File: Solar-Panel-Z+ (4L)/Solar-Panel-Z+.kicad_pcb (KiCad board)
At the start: 4 copper layers, 48.4 x 48.4 mm, 79 parts, among them J1 FTS-105-01-L-DV-A, Q1 BSS138DWQ-7, Q2 MBT2222ADW1T1, Q3 BSS138DWQ-7, Q4 MBT2222ADW1T1, U1 BQ25570RGRR, U2 TSL2561

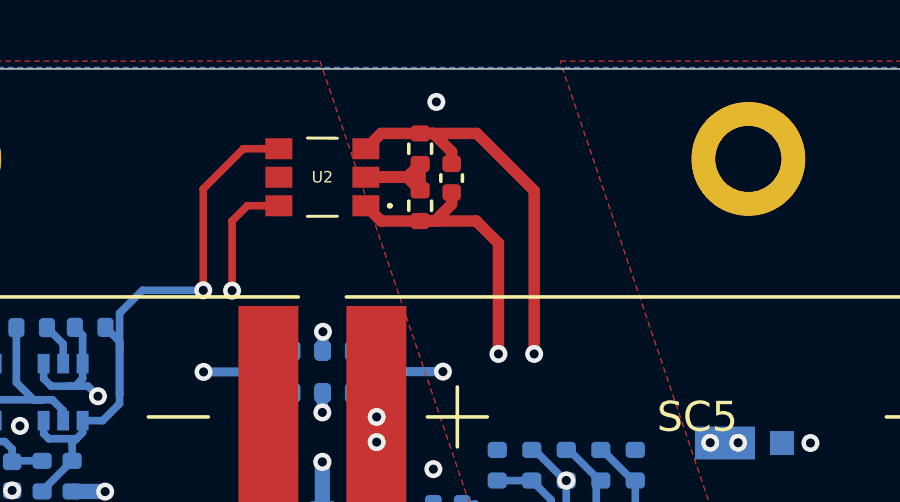
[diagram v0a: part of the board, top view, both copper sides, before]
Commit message: Added 4 Layer Z- board
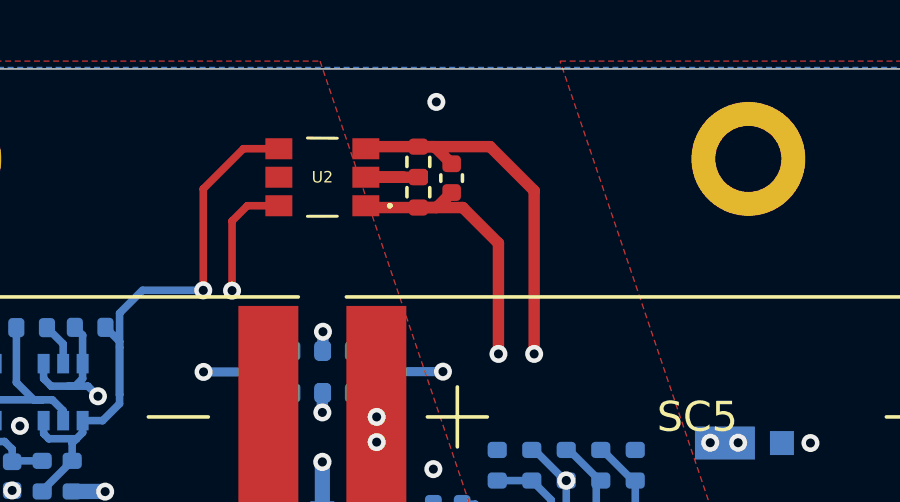
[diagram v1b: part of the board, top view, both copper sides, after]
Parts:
- moved R1 0.45 mm to (109.9, 46.4)
- moved R2 0.44 mm to (109.9, 45.4)
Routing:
- net Net-(R1-Pad1): track 4.71 -> 2.96 mm
- net GND: track 31.1 -> 30.4 mm
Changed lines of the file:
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@@
   )
   (footprint "Resistor_SMD:R_0402_1005Metric" (layer "F.Cu")
-    (at 109.96 46.86 -90)
+    (at 109.9 46.41 -90)
     (descr "Resistor SMD 0402 (1005 Metric), square (rectangular) end terminal, IPC_7351 nominal, (Body size source: IPC-SM-782 page 72, https://www.pcb-3d.com/wordpress/wp-content/uploads/ipc-sm-782a_amendment_1_and_2.pdf), generated with kicad-footprint-generator")
     (tags "resistor")
@@
   )
   (footprint "Resistor_SMD:R_0402_1005Metric" (layer "F.Cu")
-    (at 109.96 44.96 -90)
+    (at 109.9 45.4 -90)
     (descr "Resistor SMD 0402 (1005 Metric), square (rectangular) end terminal, IPC_7351 nominal, (Body size source: IPC-SM-782 page 72, https://www.pcb-3d.com/wordpress/wp-content/uploads/ipc-sm-782a_amendment_1_and_2.pdf), generated with kicad-footprint-generator")
     (tags "resistor")
@@
     (pts (xy 82.5 42.3) (xy 82.5 90.7))
     (height 2.1)
-    (gr_text "48.4000 mm" (at 79.25 66.5 90) (layer "Dwgs.User")
+    (gr_text "1905.5118 mils" (at 79.25 66.5 90) (layer "Dwgs.User")
       (effects (font (size 1 1) (thickness 0.15)))
     )
@@
     (pts (xy 82.5 42.3) (xy 130.9 42.3))
     (height -2.1)
-    (gr_text "48.4000 mm" (at 106.7 39.05) (layer "Dwgs.User")
+    (gr_text "1905.5118 mils" (at 106.7 39.05) (layer "Dwgs.User")
       (effects (font (size 1 1) (thickness 0.15)))
     )
@@
     (style (thickness 0.1) (arrow_length 1.27) (text_position_mode 0) (extension_height 0.58642) (extension_offset 0.5) keep_text_aligned)
   )
+  (segment (start 113.76 51.8) (end 113.76 46.36) (width 0.381) (layer "F.Cu") (net 1))
   (segment (start 83.9 78.7) (end 89.5 78.7) (width 0.762) (layer "F.Cu") (net 1))
-  (segment (start 108.66 44.45) (end 108.15 44.96) (width 0.381) (layer "F.Cu") (net 1))
-  (segment (start 109.96 44.45) (end 108.66 44.45) (width 0.381) (layer "F.Cu") (net 1))
-  (segment (start 113.76 46.36) (end 111.85 44.45) (width 0.381) (layer "F.Cu") (net 1))
   (segment (start 89.5 78.7) (end 91.1 78.7) (width 0.762) (layer "F.Cu") (net 1))
-  (segment (start 111.01 45.06) (end 110.4 44.45) (width 0.381) (layer "F.Cu") (net 1))
-  (segment (start 111.85 44.45) (end 109.96 44.45) (width 0.381) (layer "F.Cu") (net 1))
-  (segment (start 110.4 44.45) (end 109.96 44.45) (width 0.381) (layer "F.Cu") (net 1))
-  (segment (start 113.76 51.8) (end 113.76 46.36) (width 0.381) (layer "F.Cu") (net 1))
+  (segment (start 108.22 44.89) (end 108.15 44.96) (width 0.381) (layer "F.Cu") (net 1))
+  (segment (start 110.44 44.89) (end 109.9 44.89) (width 0.381) (layer "F.Cu") (net 1))
+  (segment (start 111.01 45.46) (end 110.44 44.89) (width 0.381) (layer "F.Cu") (net 1))
+  (segment (start 112.29 44.89) (end 109.9 44.89) (width 0.381) (layer "F.Cu") (net 1))
+  (segment (start 113.76 46.36) (end 112.29 44.89) (width 0.381) (layer "F.Cu") (net 1))
   (segment (start 90.2 78.7) (end 92 78.7) (width 0.762) (layer "F.Cu") (net 1))
+  (segment (start 109.9 44.89) (end 108.22 44.89) (width 0.381) (layer "F.Cu") (net 1))
   (segment (start 89.5 78.7) (end 90.2 78.7) (width 0.762) (layer "F.Cu") (net 1))
-  (segment (start 111.01 45.46) (end 111.01 45.06) (width 0.381) (layer "F.Cu") (net 1))
   (via (at 116.17 65.71) (size 0.6) (drill 0.3) (layers "F.Cu" "B.Cu") (free) (net 1))
   (via (at 92 78.7) (size 0.6096) (drill 0.3048) (layers "F.Cu" "B.Cu") (net 1))
@@
   (segment (start 113.158911 60.373245) (end 113.858911 60.373245) (width 0.254) (layer "B.Cu") (net 1))
   (segment (start 116.501089 60.373245) (end 115.801089 60.373245) (width 0.254) (layer "B.Cu") (net 1))
-  (segment (start 110.45 47.37) (end 109.96 47.37) (width 0.381) (layer "F.Cu") (net 2))
-  (segment (start 112.57 48.11) (end 111.83 47.37) (width 0.381) (layer "F.Cu") (net 2))
-  (segment (start 111.01 46.42) (end 111.01 46.81) (width 0.381) (layer "F.Cu") (net 2))
   (segment (start 112.57 51.8) (end 112.57 48.11) (width 0.381) (layer "F.Cu") (net 2))
-  (segment (start 111.83 47.37) (end 109.96 47.37) (width 0.381) (layer "F.Cu") (net 2))
-  (segment (start 108.66 47.37) (end 108.15 46.86) (width 0.381) (layer "F.Cu") (net 2))
-  (segment (start 109.96 47.37) (end 108.66 47.37) (width 0.381) (layer "F.Cu") (net 2))
-  (segment (start 111.01 46.81) (end 110.45 47.37) (width 0.381) (layer "F.Cu") (net 2))
+  (segment (start 111.01 46.42) (end 110.51 46.92) (width 0.381) (layer "F.Cu") (net 2))
+  (segment (start 111.38 46.92) (end 108.21 46.92) (width 0.381) (layer "F.Cu") (net 2))
+  (segment (start 110.51 46.92) (end 109.9 46.92) (width 0.381) (layer "F.Cu") (net 2))
+  (segment (start 112.57 48.11) (end 111.38 46.92) (width 0.381) (layer "F.Cu") (net 2))
+  (segment (start 108.21 46.92) (end 108.15 46.86) (width 0.381) (layer "F.Cu") (net 2))
   (via (at 99.46 56.39) (size 0.6) (drill 0.3) (layers "F.Cu" "B.Cu") (net 2))
   (via (at 112.57 51.8) (size 0.6) (drill 0.3) (layers "F.Cu" "B.Cu") (net 2))
@@
   (segment (start 98.66 61.89) (end 99.52 61.03) (width 0.254) (layer "B.Cu") (net 37))
   (segment (start 97.36 62.386089) (end 97.36 61.89) (width 0.254) (layer "B.Cu") (net 37))
-  (segment (start 109.52 45.91) (end 108.15 45.91) (width 0.381) (layer "F.Cu") (net 38))
-  (segment (start 109.96 45.47) (end 109.96 46.35) (width 0.381) (layer "F.Cu") (net 38))
-  (segment (start 109.96 46.35) (end 109.52 45.91) (width 0.381) (layer "F.Cu") (net 38))
+  (segment (start 109.9 45.91) (end 108.15 45.91) (width 0.381) (layer "F.Cu") (net 38))
   (segment (start 109.419997 45.910003) (end 108.209203 45.910003) (width 0.381) (layer "F.Cu") (net 38))
-  (segment (start 109.96 45.47) (end 109.519997 45.910003) (width 0.381) (layer "F.Cu") (net 38))
   (via (at 92.65 70.95) (size 0.6096) (drill 0.3048) (layers "F.Cu" "B.Cu") (net 40))
   (via (at 114.27 63.38) (size 0.6096) (drill 0.3048) (layers "F.Cu" "B.Cu") (net 40))

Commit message: Z board updates
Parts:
- moved TP1 0.79 mm to (120.9, 77.1)
- moved TP3 0.79 mm to (120.9, 70.1)
- moved TP2 0.79 mm to (120.9, 74.7)
- moved TP4 0.79 mm to (120.9, 72.4)
- moved R16 0.32 mm to (112.0, 67.8)
- moved C2 0.10 mm to (106.7, 67.3)
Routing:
- net GND: track 30.4 -> 23.5 mm
- net VBAT: track 46.1 -> 43.9 mm
- net SCL_LS: track 21.0 -> 19.1 mm
- net Net-(R14-Pad1): track 12.9 -> 12.3 mm
- net Net-(C7-Pad1): track 0.59 -> 0.00 mm
- net /VSOLAR_FULL: track 26.9 -> 26.4 mm
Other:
- board text added: "[BAT <-> USB]"

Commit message: Exported Gerbers
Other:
- board text added: "08-AUG-2022"
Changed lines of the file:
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@@
       (drillshape 0)
       (scaleselection 1)
-      (outputdirectory "../../Z+/")
+      (outputdirectory "../gerbers/Gerbers Z+ (4L) (08-08-2022)/")
     )
   )
@@
     (effects (font (size 1.143 1.143) (thickness 0.2032)) (justify mirror))
   )
+  (gr_text "08-AUG-2022" (at 112.395 85.4456) (layer "B.SilkS")
+    (effects (font (size 0.508 0.508) (thickness 0.1016)) (justify mirror))
+  )
   (gr_text "Cable Pinout\n1.BATT_P\n2.VUSB\n3.BURN1\n4.BURN2\n5.COIL_P\n6.COIL_N\n7.SDA\n8.SCL\n9.+3V3\n10.GND" (at 90.3 70.5) (layer "B.SilkS")
     (effects (font (size 0.635 0.635) (thickness 0.0762)) (justify left mirror))
@@
   (segment (start 114.830005 61.102156) (end 114.830005 61.89) (width 0.3048) (layer "B.Cu") (net 40))
   (zone (net 26) (net_name "Net-(D3-Pad1)") (layer "F.Cu") (hatch edge 0.508)
-    (connect_pads yes (clearance 0.127))
+    (connect_pads yes (clearance 0.1524))
     (min_thickness 0.254) (filled_areas_thickness no)
     (fill yes (thermal_gap 0.508) (thermal_bridge_width 0.508))
@@
   )
   (zone (net 23) (net_name "/VSOLAR_FULL") (layer "F.Cu") (hatch edge 0.508)
-    (connect_pads yes (clearance 0.127))
+    (connect_pads yes (clearance 0.1524))
     (min_thickness 0.254) (filled_areas_thickness no)
     (fill yes (thermal_gap 0.508) (thermal_bridge_width 0.508))
@@
   )
   (zone (net 1) (net_name "GND") (layer "F.Cu") (hatch edge 0.508)
-    (connect_pads yes (clearance 0.127))
+    (connect_pads yes (clearance 0.1524))
     (min_thickness 0.254) (filled_areas_thickness no)
     (fill yes (thermal_gap 0.508) (thermal_bridge_width 0.508))
@@
   )
   (zone (net 2) (net_name "+3V3") (layer "In1.Cu") (hatch edge 0.508)
-    (connect_pads yes (clearance 0))
+    (connect_pads yes (clearance 0.1524))
     (min_thickness 0.254) (filled_areas_thickness no)
     (fill yes (thermal_gap 0.508) (thermal_bridge_width 0.508))
@@
   (zone (net 6) (net_name "VSOLAR") (layer "B.Cu") (hatch edge 0.508)
     (priority 4)
-    (connect_pads yes (clearance 0.127))
-    (min_thickness 0.127) (filled_areas_thickness no)
-    (fill yes (thermal_gap 0.127) (thermal_bridge_width 0.2286))
+    (connect_pads yes (clearance 0.1524))
+    (min_thickness 0.254) (filled_areas_thickness no)
+    (fill yes (thermal_gap 0.254) (thermal_bridge_width 0.254))
     (polygon
       (pts
@@
   (zone (net 13) (net_name "Net-(C10-Pad1)") (layer "B.Cu") (hatch edge 0.508)
     (priority 6)
-    (connect_pads yes (clearance 0.127))
-    (min_thickness 0.127) (filled_areas_thickness no)
-    (fill yes (thermal_gap 0.127) (thermal_bridge_width 0.2286))
+    (connect_pads yes (clearance 0.1524))
+    (min_thickness 0.254) (filled_areas_thickness no)
+    (fill yes (thermal_gap 0.254) (thermal_bridge_width 0.254))
     (polygon
       (pts
@@
   (zone (net 14) (net_name "Net-(L2-Pad1)") (layer "B.Cu") (hatch edge 0.508)
     (priority 4)
-    (connect_pads yes (clearance 0.000001))
-    (min_thickness 0.2032) (filled_areas_thickness no)
+    (connect_pads yes (clearance 0.1524))
+    (min_thickness 0.254) (filled_areas_thickness no)
     (fill yes (thermal_gap 0.508) (thermal_bridge_width 0.508))
     (polygon
@@
   (zone (net 4) (net_name "Net-(L1-Pad2)") (layer "B.Cu") (hatch edge 0.508)
     (priority 6)
-    (connect_pads yes (clearance 0.000001))
-    (min_thickness 0.2032) (filled_areas_thickness no)
+    (connect_pads yes (clearance 0.1524))
+    (min_thickness 0.254) (filled_areas_thickness no)
     (fill yes (thermal_gap 0.508) (thermal_bridge_width 0.508))
     (polygon
@@
   (zone (net 3) (net_name "Net-(C7-Pad1)") (layer "B.Cu") (hatch edge 0.508)
     (priority 4)
-    (connect_pads yes (clearance 0.127))
-    (min_thickness 0.127) (filled_areas_thickness no)
-    (fill yes (thermal_gap 0.127) (thermal_bridge_width 0.2286))
+    (connect_pads yes (clearance 0.1524))
+    (min_thickness 0.254) (filled_areas_thickness no)
+    (fill yes (thermal_gap 0.254) (thermal_bridge_width 0.254))
     (polygon
       (pts
         (xy 114.68079 62.754956)
-        (xy 114.68079 68.36)
-        (xy 112.32924 68.36)
-        (xy 112.32924 67.1124)
+        (xy 114.68079 68.1822)
+        (xy 112.20224 68.1822)
+        (xy 112.20224 67.1124)
         (xy 112.7164 67.1124)
         (xy 112.7164 63.01)
@@
   )
   (zone (net 1) (net_name "GND") (layers "In2.Cu" "B.Cu") (hatch edge 0.508)
-    (connect_pads yes (clearance 0))
+    (connect_pads yes (clearance 0.1524))
     (min_thickness 0.254) (filled_areas_thickness no)
     (fill yes (thermal_gap 0.508) (thermal_bridge_width 0.508))
